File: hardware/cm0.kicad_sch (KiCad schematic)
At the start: 0 parts

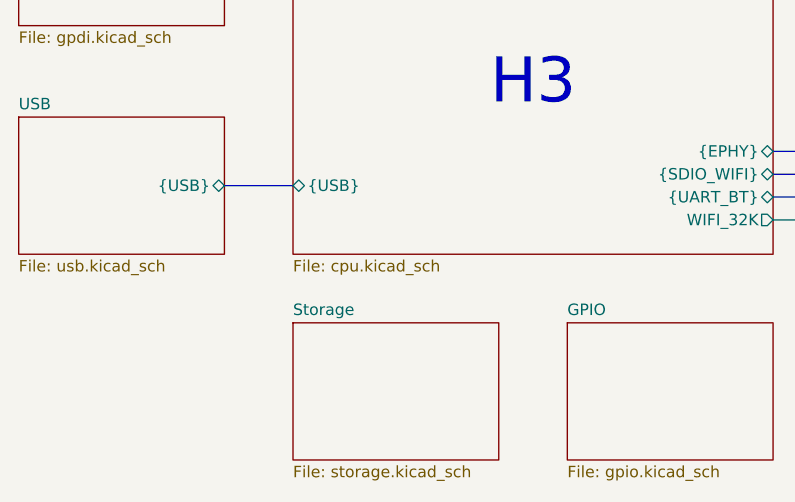
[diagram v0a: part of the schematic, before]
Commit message: Add eMMC and uSD
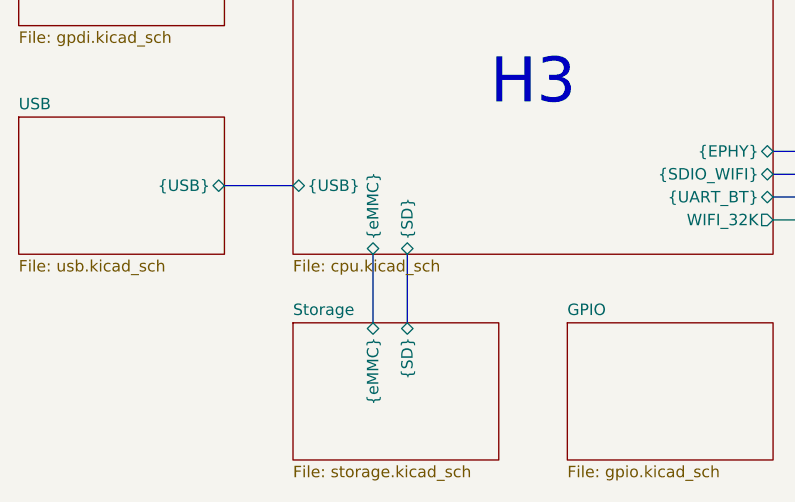
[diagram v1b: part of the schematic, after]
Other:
- sheet H3 ports: added {SD}, {eMMC}; removed none
- sheet Storage ports: added {SD}, {eMMC}; removed none
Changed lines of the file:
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@@
+	(bus
+		(pts
+			(xy 125.73 123.19) (xy 125.73 130.81)
+		)
+		(stroke
+			(width 0)
+			(type default)
+		)
+	)
 	(bus
 		(pts
@@
 		(pts
 			(xy 166.37 91.44) (xy 173.99 91.44)
+		)
+		(stroke
+			(width 0)
+			(type default)
+		)
+	)
+	(bus
+		(pts
+			(xy 121.92 123.19) (xy 121.92 130.81)
 		)
 		(stroke
@@
 			)
 		)
+		(pin "{eMMC}" bidirectional
+			(at 121.92 130.81 90)
+			(effects
+				(font
+					(size 1.27 1.27)
+				)
+				(justify right)
+			)
+		)
+		(pin "{SD}" bidirectional
+			(at 125.73 130.81 90)
+			(effects
+				(font
+					(size 1.27 1.27)
+				)
+				(justify right)
+			)
+		)
 		(instances
 			(project "cm0"
@@
 			)
 		)
+		(pin "{eMMC}" bidirectional
+			(at 121.92 123.19 270)
+			(effects
+				(font
+					(size 1.27 1.27)
+				)
+				(justify left)
+			)
+		)
+		(pin "{SD}" bidirectional
+			(at 125.73 123.19 270)
+			(effects
+				(font
+					(size 1.27 1.27)
+				)
+				(justify left)
+			)
+		)
